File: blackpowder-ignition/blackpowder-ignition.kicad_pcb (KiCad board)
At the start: 2 copper layers, 63.5 x 63.5 mm, 7 parts, among them J1 CAS_stacking, J2 Conn_02x01, Q1 FDS6898A

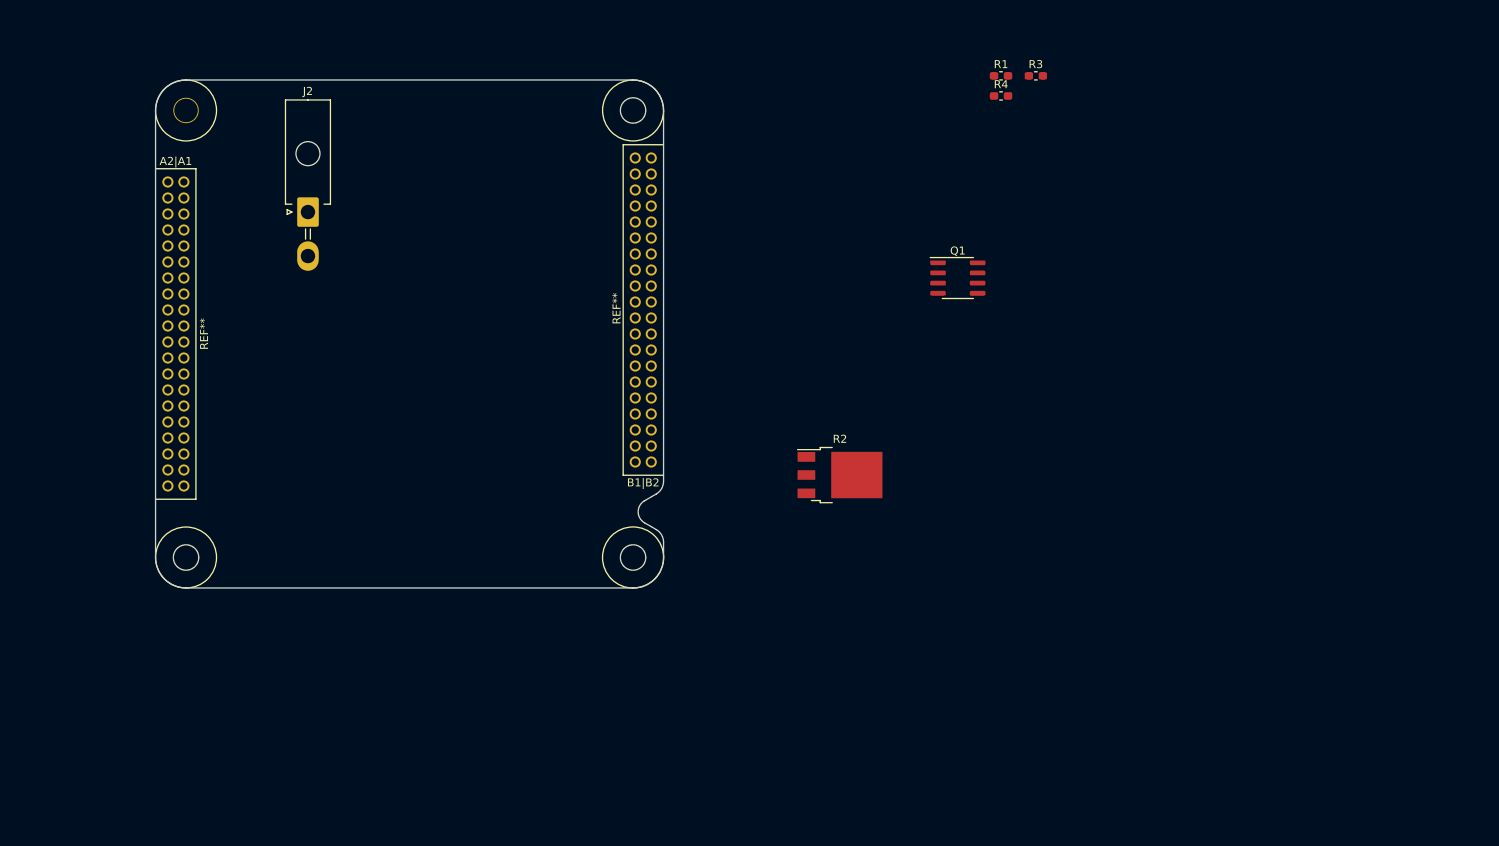
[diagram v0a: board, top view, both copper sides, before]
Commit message: made hierarchical block for individual ignition circuit
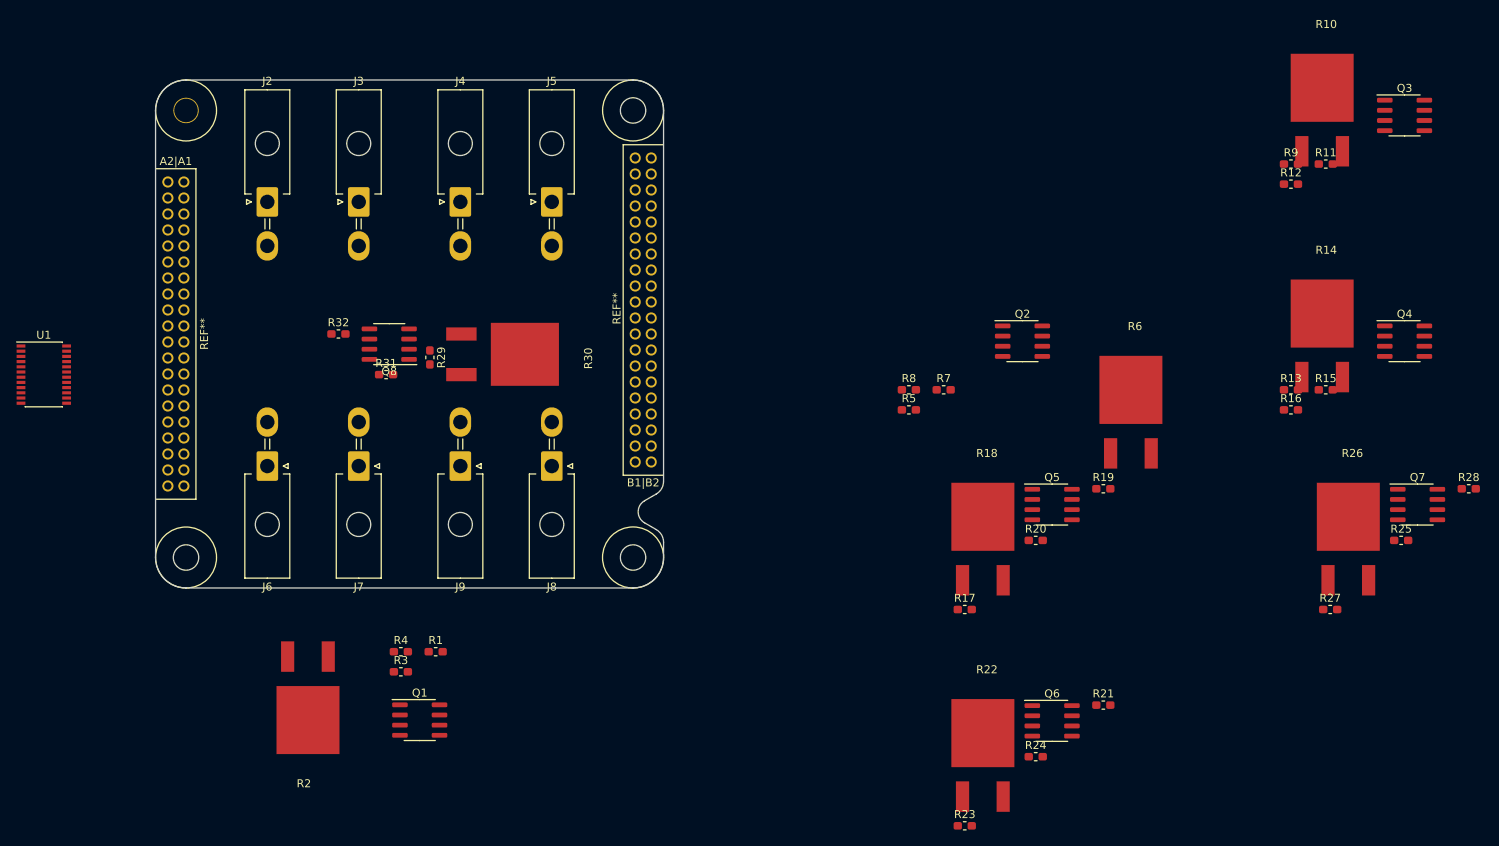
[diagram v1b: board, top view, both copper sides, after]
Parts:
- added J3: Conn_01x02, Connector_Molex:Molex_Mini-Fit_Jr_5569-02A2_2x01_P4.20mm_Horizontal, F.Cu at (146.1, 88.9)
- added J4: Conn_01x02, Connector_Molex:Molex_Mini-Fit_Jr_5569-02A2_2x01_P4.20mm_Horizontal, F.Cu at (158.8, 88.9)
- added J5: Conn_01x02, Connector_Molex:Molex_Mini-Fit_Jr_5569-02A2_2x01_P4.20mm_Horizontal, F.Cu at (170.2, 88.9)
- added J6: Conn_01x02, Connector_Molex:Molex_Mini-Fit_Jr_5569-02A2_2x01_P4.20mm_Horizontal, F.Cu at (134.6, 121.9)
- added J7: Conn_01x02, Connector_Molex:Molex_Mini-Fit_Jr_5569-02A2_2x01_P4.20mm_Horizontal, F.Cu at (146.1, 121.9)
- added J8: Conn_01x02, Connector_Molex:Molex_Mini-Fit_Jr_5569-02A2_2x01_P4.20mm_Horizontal, F.Cu at (170.2, 121.9)
- added J9: Conn_01x02, Connector_Molex:Molex_Mini-Fit_Jr_5569-02A2_2x01_P4.20mm_Horizontal, F.Cu at (158.8, 121.9)
- added Q2: FDS6898A, Package_SO:SOIC-8_3.9x4.9mm_P1.27mm, F.Cu at (229.0, 106.3)
- added Q3: FDS6898A, Package_SO:SOIC-8_3.9x4.9mm_P1.27mm, F.Cu at (276.8, 78.1)
- added Q4: FDS6898A, Package_SO:SOIC-8_3.9x4.9mm_P1.27mm, F.Cu at (276.8, 106.3)
- added Q5: FDS6898A, Package_SO:SOIC-8_3.9x4.9mm_P1.27mm, F.Cu at (232.7, 126.7)
- added Q6: FDS6898A, Package_SO:SOIC-8_3.9x4.9mm_P1.27mm, F.Cu at (232.7, 153.8)
- added Q7: FDS6898A, Package_SO:SOIC-8_3.9x4.9mm_P1.27mm, F.Cu at (278.4, 126.7)
- added Q8: FDS6898A, Package_SO:SOIC-8_3.9x4.9mm_P1.27mm, F.Cu at (149.9, 106.7)
- added R10: R, star-common-lib:PWR163, F.Cu at (266.5, 78.9)
- added R11: R, Resistor_SMD:R_0603_1608Metric_Pad1.05x0.95mm_HandSolder, F.Cu at (266.9, 84.2)
- added R12: R, Resistor_SMD:R_0603_1608Metric_Pad1.05x0.95mm_HandSolder, F.Cu at (262.6, 86.7)
- added R13: R, Resistor_SMD:R_0603_1608Metric_Pad1.05x0.95mm_HandSolder, F.Cu at (262.6, 112.4)
- added R14: R, star-common-lib:PWR163, F.Cu at (266.5, 107.1)
- added R15: R, Resistor_SMD:R_0603_1608Metric_Pad1.05x0.95mm_HandSolder, F.Cu at (266.9, 112.4)
- added R16: R, Resistor_SMD:R_0603_1608Metric_Pad1.05x0.95mm_HandSolder, F.Cu at (262.6, 114.9)
- added R17: R, Resistor_SMD:R_0603_1608Metric_Pad1.05x0.95mm_HandSolder, F.Cu at (221.8, 139.8)
- added R18: R, star-common-lib:PWR163, F.Cu at (224.1, 132.5)
- added R19: R, Resistor_SMD:R_0603_1608Metric_Pad1.05x0.95mm_HandSolder, F.Cu at (239.1, 124.8)
- added R20: R, Resistor_SMD:R_0603_1608Metric_Pad1.05x0.95mm_HandSolder, F.Cu at (230.7, 131.2)
- added R21: R, Resistor_SMD:R_0603_1608Metric_Pad1.05x0.95mm_HandSolder, F.Cu at (239.1, 151.8)
- added R22: R, star-common-lib:PWR163, F.Cu at (224.1, 159.6)
- added R23: R, Resistor_SMD:R_0603_1608Metric_Pad1.05x0.95mm_HandSolder, F.Cu at (221.8, 166.9)
- added R24: R, Resistor_SMD:R_0603_1608Metric_Pad1.05x0.95mm_HandSolder, F.Cu at (230.7, 158.2)
- added R25: R, Resistor_SMD:R_0603_1608Metric_Pad1.05x0.95mm_HandSolder, F.Cu at (276.4, 131.2)
- added R26: R, star-common-lib:PWR163, F.Cu at (269.7, 132.5)
- added R27: R, Resistor_SMD:R_0603_1608Metric_Pad1.05x0.95mm_HandSolder, F.Cu at (267.5, 139.8)
- added R28: R, Resistor_SMD:R_0603_1608Metric_Pad1.05x0.95mm_HandSolder, F.Cu at (284.8, 124.8)
- added R29: R, Resistor_SMD:R_0603_1608Metric_Pad1.05x0.95mm_HandSolder, F.Cu at (154.9, 108.3)
- added R30: R, star-common-lib:PWR163, F.Cu at (162.6, 108.0)
- added R31: R, Resistor_SMD:R_0603_1608Metric_Pad1.05x0.95mm_HandSolder, F.Cu at (149.5, 110.5)
- added R32: R, Resistor_SMD:R_0603_1608Metric_Pad1.05x0.95mm_HandSolder, F.Cu at (143.5, 105.4)
- added R5: R, Resistor_SMD:R_0603_1608Metric_Pad1.05x0.95mm_HandSolder, F.Cu at (214.8, 114.9)
- added R6: R, star-common-lib:PWR163, F.Cu at (242.6, 116.6)
- added R7: R, Resistor_SMD:R_0603_1608Metric_Pad1.05x0.95mm_HandSolder, F.Cu at (219.2, 112.4)
- added R8: R, Resistor_SMD:R_0603_1608Metric_Pad1.05x0.95mm_HandSolder, F.Cu at (214.8, 112.4)
- added R9: R, Resistor_SMD:R_0603_1608Metric_Pad1.05x0.95mm_HandSolder, F.Cu at (262.6, 84.2)
- added U1: TCA9555PWR, Package_SO:TSSOP-24_4.4x7.8mm_P0.65mm, F.Cu at (106.7, 110.5)
- J2: value Conn_02x01 -> Conn_01x02
- R2: footprint Package_TO_SOT_SMD:TO-252-3_TabPin2 -> star-common-lib:PWR163
- moved R3 108.9 mm to (151.3, 147.6)
- moved R4 102.2 mm to (151.3, 145.1)
- moved R1 100.9 mm to (155.7, 145.1)
- moved Q1 87.0 mm to (153.7, 153.7)
- moved R2 71.5 mm to (139.7, 149.4), turned to 180 degrees
- moved J2 5.24 mm to (134.6, 88.9)
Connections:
- net igniteA renamed /IgnitionA/ignite
- net ~contA~ renamed /IgnitionA/~cont~

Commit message: added hierarchical sch sheet for bus, address jummper pads, connections from io expander to subcircuits
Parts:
- removed J8, J9: Conn_01x02, Connector_Molex:Molex_Mini-Fit_Jr_5569-02A2_2x01_P4.20mm_Horizontal
- removed Q7, Q8: FDS6898A, Package_SO:SOIC-8_3.9x4.9mm_P1.27mm
- removed R25, R27, R28, R29, R31, R32: R, Resistor_SMD:R_0603_1608Metric_Pad1.05x0.95mm_HandSolder
- removed R26, R30: R, star-common-lib:PWR163
- added JP1: SolderJumper_3_Bridged12, Jumper:SolderJumper-3_P1.3mm_Bridged12_RoundedPad1.0x1.5mm, F.Cu at (190.5, 61.0)
- added JP2: SolderJumper_3_Bridged12, Jumper:SolderJumper-3_P1.3mm_Bridged12_RoundedPad1.0x1.5mm, F.Cu at (196.8, 67.3)
- added JP3: SolderJumper_3_Bridged12, Jumper:SolderJumper-3_P1.3mm_Bridged12_RoundedPad1.0x1.5mm, F.Cu at (202.5, 63.5)
- moved J1 74.2 mm to (48.3, 57.1)
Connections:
- net Net-(J1-PadA1) renamed /CAS_bus/INT1
- net Net-(J1-PadA10) renamed /CAS_bus/INT4
- net Net-(J1-PadA11) renamed /CAS_bus/INT5
- net Net-(J1-PadA12) renamed /CAS_bus/INT6
- net Net-(J1-PadA17) renamed /CAS_bus/I2C1_SCL
- net Net-(J1-PadA18) renamed /CAS_bus/I2C1_SDA
- net Net-(J1-PadA19) renamed /CAS_bus/INT7
- net Net-(J1-PadA2) renamed /CAS_bus/INT2
- net Net-(J1-PadA20) renamed /CAS_bus/INT8
- net Net-(J1-PadA21) renamed /CAS_bus/SPI0_nSS1
- net Net-(J1-PadA22) renamed /CAS_bus/SPI0_nSS2
- net Net-(J1-PadA23) renamed /CAS_bus/SPI0_SCK
- net Net-(J1-PadA24) renamed /CAS_bus/SPI0_nSS3
- net Net-(J1-PadA26) renamed /CAS_bus/SPI0_nSS4
- net Net-(J1-PadA27) renamed /CAS_bus/SPI0_MISO
- net Net-(J1-PadA28) renamed /CAS_bus/SPI0_nSS5
- net Net-(J1-PadA30) renamed /CAS_bus/SPI0_nSS6
- net Net-(J1-PadA31) renamed /CAS_bus/SPI0_MOSI
- net Net-(J1-PadA32) renamed /CAS_bus/SPI0_nSS7
- net Net-(J1-PadA34) renamed /CAS_bus/SPI0_nSS8
- net Net-(J1-PadA9) renamed /CAS_bus/INT3
- net Net-(J1-PadB1) renamed /CAS_bus/SPIHS_SCK
- net Net-(J1-PadB13) renamed /CAS_bus/SPIHS_nSS1
- net Net-(J1-PadB14) renamed /CAS_bus/SPIHS_nSS2
- net Net-(J1-PadB6) renamed /CAS_bus/SPIHS_MISO
- net Net-(J1-PadB9) renamed /CAS_bus/SPIHS_MOSI
- J1 pad A13: Net-(J1-PadA13) -> /CAS_bus/I2C0_SCL
- J1 pad A14: Net-(J1-PadA14) -> /CAS_bus/I2C0_SDA
- J1 pad A15: Net-(J1-PadA15) -> GND
- J1 pad A16: Net-(J1-PadA16) -> GND
- J1 pad A25: Net-(J1-PadA25) -> GND
- J1 pad A29: Net-(J1-PadA29) -> GND
- J1 pad A3: Net-(J1-PadA3) -> GND
- J1 pad A33: Net-(J1-PadA33) -> GND
- J1 pad A35: Net-(J1-PadA35) -> +3V3
- J1 pad A36: Net-(J1-PadA36) -> +3V3
- J1 pad A37: Net-(J1-PadA37) -> GND
- J1 pad A38: Net-(J1-PadA38) -> GND
- J1 pad A39: Net-(J1-PadA39) -> +BATT
- J1 pad A4: Net-(J1-PadA4) -> GND
- J1 pad A40: Net-(J1-PadA40) -> +BATT
- J1 pad A5: Net-(J1-PadA5) -> +5V
- J1 pad A6: Net-(J1-PadA6) -> +5V
- J1 pad A7: Net-(J1-PadA7) -> GND
- J1 pad A8: Net-(J1-PadA8) -> GND
- J1 pad B10: Net-(J1-PadB10) -> GND
- J1 pad B11: Net-(J1-PadB11) -> GND
- J1 pad B12: Net-(J1-PadB12) -> GND
- J1 pad B2: Net-(J1-PadB2) -> GND
- J1 pad B3: Net-(J1-PadB3) -> GND
- J1 pad B4: Net-(J1-PadB4) -> GND
- J1 pad B5: Net-(J1-PadB5) -> GND
- J1 pad B7: Net-(J1-PadB7) -> GND
- J1 pad B8: Net-(J1-PadB8) -> GND
- Q1 pad 2: /IgnitionA/ignite -> igniteA
- Q1 pad 5: /IgnitionA/~cont~ -> ~contA~
- Q1 pad 6: /IgnitionA/~cont~ -> ~contA~
- Q2 pad 2: /ignitionB/ignite -> igniteB
- Q2 pad 5: /ignitionB/~cont~ -> ~contB~
- Q2 pad 6: /ignitionB/~cont~ -> ~contB~
- Q3 pad 2: /ignitionC/ignite -> igniteC
- Q3 pad 5: /ignitionC/~cont~ -> ~contC~
- Q3 pad 6: /ignitionC/~cont~ -> ~contC~
- Q4 pad 2: /ignitionD/ignite -> igniteD
- Q4 pad 5: /ignitionD/~cont~ -> ~contD~
- Q4 pad 6: /ignitionD/~cont~ -> ~contD~
- Q5 pad 2: /sheet5EB223DF/ignite -> igniteE
- Q5 pad 5: /sheet5EB223DF/~cont~ -> ~contE~
- Q5 pad 6: /sheet5EB223DF/~cont~ -> ~contE~
- Q6 pad 2: /sheet5EB223E0/ignite -> igniteF
- Q6 pad 5: /sheet5EB223E0/~cont~ -> ~contF~
- Q6 pad 6: /sheet5EB223E0/~cont~ -> ~contF~
- R1 pad 1: /IgnitionA/ignite -> igniteA
- R12 pad 2: /ignitionC/~cont~ -> ~contC~
- R13 pad 1: /ignitionD/ignite -> igniteD
- R16 pad 2: /ignitionD/~cont~ -> ~contD~
- R17 pad 1: /sheet5EB223DF/ignite -> igniteE
- R20 pad 2: /sheet5EB223DF/~cont~ -> ~contE~
- R21 pad 1: /sheet5EB223E0/ignite -> igniteF
- R24 pad 2: /sheet5EB223E0/~cont~ -> ~contF~
- R4 pad 2: /IgnitionA/~cont~ -> ~contA~
- R5 pad 1: /ignitionB/ignite -> igniteB
- R8 pad 2: /ignitionB/~cont~ -> ~contB~
- R9 pad 1: /ignitionC/ignite -> igniteC
- U1 pad 10: Net-(U1-Pad10) -> igniteD
- U1 pad 11: Net-(U1-Pad11) -> ~contD~
- U1 pad 12: Net-(U1-Pad12) -> GND
- U1 pad 13: Net-(U1-Pad13) -> igniteE
- U1 pad 14: Net-(U1-Pad14) -> ~contE~
- U1 pad 15: Net-(U1-Pad15) -> igniteF
- U1 pad 16: Net-(U1-Pad16) -> ~contF~
- U1 pad 2: Net-(U1-Pad2) -> A1
- U1 pad 21: Net-(U1-Pad21) -> A0
- U1 pad 22: Net-(U1-Pad22) -> /CAS_bus/I2C0_SCL
- U1 pad 23: Net-(U1-Pad23) -> /CAS_bus/I2C0_SDA
- U1 pad 24: Net-(U1-Pad24) -> +3V3
- U1 pad 3: Net-(U1-Pad3) -> A2
- U1 pad 4: Net-(U1-Pad4) -> igniteA
- U1 pad 5: Net-(U1-Pad5) -> ~contA~
- U1 pad 6: Net-(U1-Pad6) -> igniteB
- U1 pad 7: Net-(U1-Pad7) -> ~contB~
- U1 pad 8: Net-(U1-Pad8) -> igniteC
- U1 pad 9: Net-(U1-Pad9) -> ~contC~

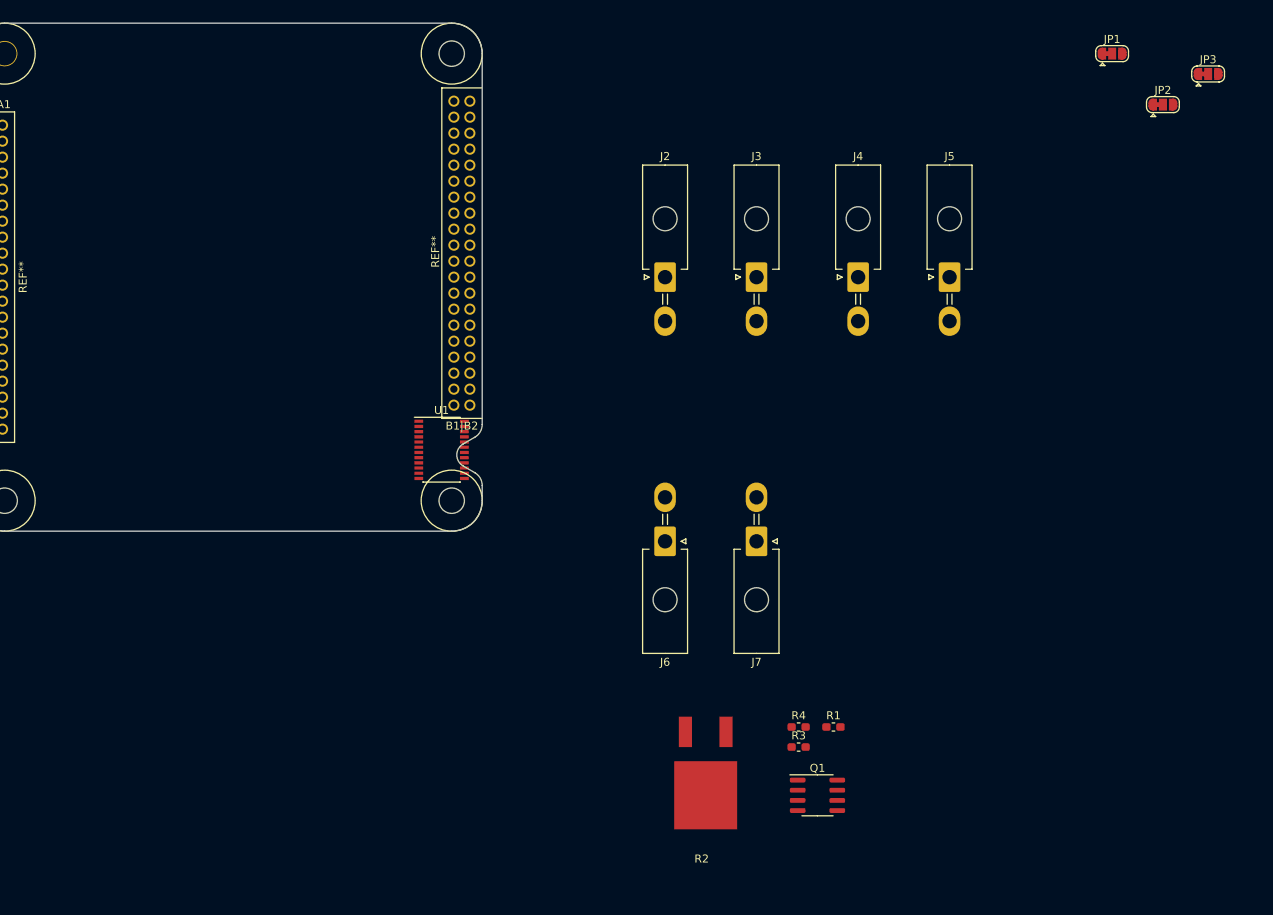
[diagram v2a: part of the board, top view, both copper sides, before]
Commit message: added power connector
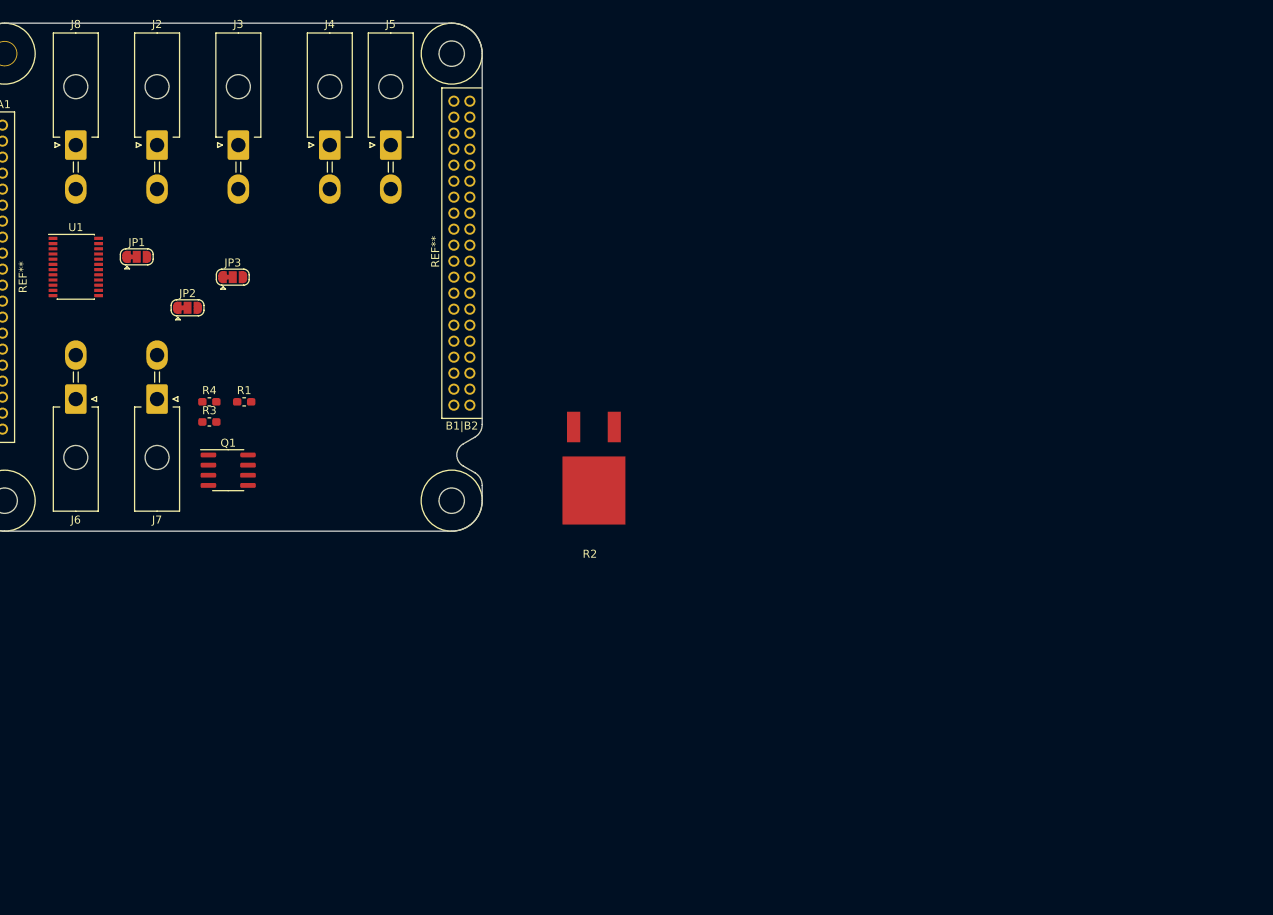
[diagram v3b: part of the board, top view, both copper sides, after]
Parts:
- added J8: Conn_01x02, Connector_Molex:Molex_Mini-Fit_Jr_5569-02A2_2x01_P4.20mm_Horizontal, F.Cu at (61.0, 72.4)
- moved JP1 124.5 mm to (68.6, 86.4)
- moved JP3 124.5 mm to (80.6, 88.9)
- moved JP2 124.5 mm to (74.9, 92.7)
- moved R3 84.1 mm to (77.7, 107.0)
- moved Q1 84.1 mm to (80.0, 113.0)
- moved R1 84.1 mm to (82.0, 104.5)
- moved R4 84.1 mm to (77.7, 104.5)
- moved J7 77.0 mm to (71.1, 104.1)
- moved J6 75.8 mm to (61.0, 104.1)
- moved J5 71.8 mm to (100.3, 72.4)
- moved J4 68.1 mm to (92.7, 72.4)
- moved J3 66.8 mm to (81.3, 72.4)
- moved J2 65.6 mm to (71.1, 72.4)
- moved U1 51.1 mm to (61.0, 87.6)
- moved R2 40.6 mm to (125.7, 111.3)

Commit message: initial layout
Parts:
- added C1: 100nF, Capacitor_SMD:C_0603_1608Metric_Pad1.05x0.95mm_HandSolder, F.Cu at (62.6, 103.8)
- R1, R11, R13, R15, R3, R5, R7, R9: moved to B.Cu
- moved J6 243.3 mm to (303.4, 124.6), turned to 0 degrees
- moved J7 237.8 mm to (303.4, 155.1), turned to 0 degrees
- moved R12 184.3 mm to (78.5, 95.8), turned to 180 degrees
- moved Q3 182.2 mm to (94.8, 68.8), turned to 180 degrees
- moved R16 180.1 mm to (83.8, 92.7), turned to 180 degrees
- moved Q4 175.6 mm to (105.2, 68.7), turned to 180 degrees
- moved R10 173.3 mm to (93.2, 78.0), turned to 180 degrees
- moved R11 172.6 mm to (95.1, 67.7), turned to 270 degrees
- moved R15 167.4 mm to (105.6, 67.7), turned to 270 degrees
- moved R9 165.9 mm to (97.4, 69.0), turned to 90 degrees
- moved R14 165.2 mm to (103.8, 78.0), turned to 180 degrees
- moved R6 164.4 mm to (82.8, 78.0), turned to 180 degrees
- moved R13 160.8 mm to (107.8, 68.9), turned to 90 degrees
- moved Q2 149.8 mm to (83.9, 68.8), turned to 180 degrees
- moved R7 141.9 mm to (84.5, 67.8), turned to 270 degrees
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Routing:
- net GND: track 0.00 -> 208.2 mm
- net ~contB~: track 0.00 -> 51.1 mm, vias 0 -> 2
- net igniteD: track 0.00 -> 50.8 mm, vias 0 -> 2
- net +3V3: track 0.00 -> 50.8 mm
- net ~contD~: track 0.00 -> 49.6 mm, vias 0 -> 2
- net ~contC~: track 0.00 -> 47.5 mm, vias 0 -> 2
- net ~contA~: track 0.00 -> 46.4 mm, vias 0 -> 2
- net igniteC: track 0.00 -> 45.6 mm, vias 0 -> 2
- net igniteB: track 0.00 -> 40.3 mm, vias 0 -> 2
- net igniteA: track 0.00 -> 40.2 mm, vias 0 -> 2
- net +BATT: track 0.00 -> 38.6 mm
- net /CAS_bus/I2C0_SDA: track 0.00 -> 37.1 mm
- net /CAS_bus/I2C0_SCL: track 0.00 -> 35.3 mm
- net Net-(J2-Pad2): track 0.00 -> 15.9 mm
- net Net-(J3-Pad2): track 0.00 -> 15.4 mm
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- added copper zone on B.Cu, net GND
- added copper zone on F.Cu, net Net-(Q1-Pad4)
- added copper zone on F.Cu, net Net-(Q2-Pad4)
- added copper zone on F.Cu, net Net-(Q3-Pad4)
- added copper zone on F.Cu, net Net-(Q4-Pad4)
- added copper zone on F.Cu, net ~contA~
- added copper zone on F.Cu, net ~contB~
- added copper zone on F.Cu, net ~contC~
- added copper zone on F.Cu, net ~contD~
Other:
- net class Default: clearance 0.2 -> 0.1524; trace_width 0.25 -> 0.2032
- net class Ignition added: clearance 0.60452, trace_width 0.762, via_dia 0.8, via_drill 0.4
- rule pad_to_mask_clearance: 0.051 -> 0
- rule trace_clearance: 0.2 -> 0.1524
